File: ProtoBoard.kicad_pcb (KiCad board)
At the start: 4 copper layers, 50 x 35 mm, 52 parts, among them IC1 L9110S, IC2 L9110S, IC3 L9110S, J1 Conn_01x02_Female, J11 Conn_01x10_Female, J2 Conn_01x08_Female, J3 I2C_STANDARDQWIIC, J4 Conn_01x10_Female, J5 Conn_01x05_Female, J6 Conn_01x05_Female, J7 Conn_01x10_Female, J8 Conn_01x05_Female, J9 Conn_01x10_Female, U1 ESP32-WROOM-32D, U10 SY6280AAC, U2 CD74HC4067SM, U3 LM1084-5.0, U4 CD74HC4067SM, U6 LM1084-3.3, U7 SY6280AAC, U8 SY6280AAC, U9 SY6280AAC

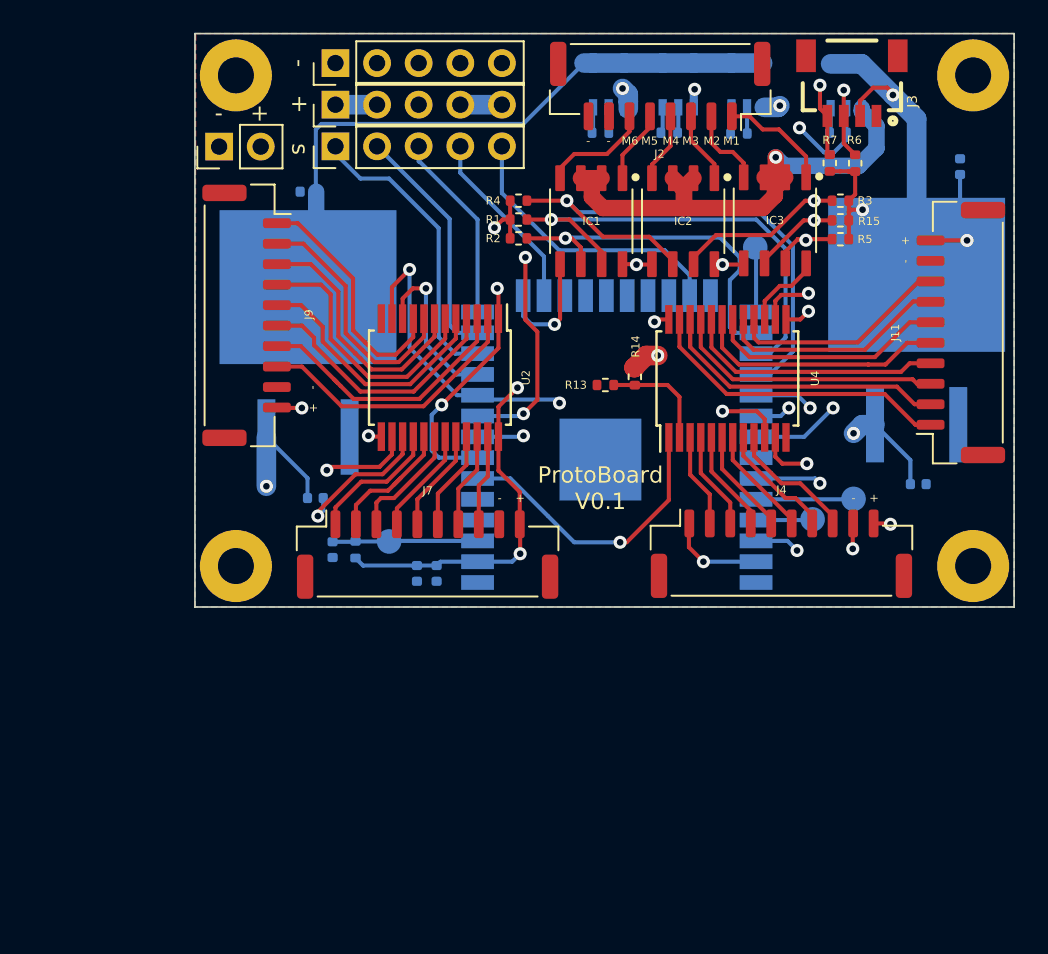
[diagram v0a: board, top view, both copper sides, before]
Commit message: Add bms + switch to esp32s3 + USB C + 8 LRA driver
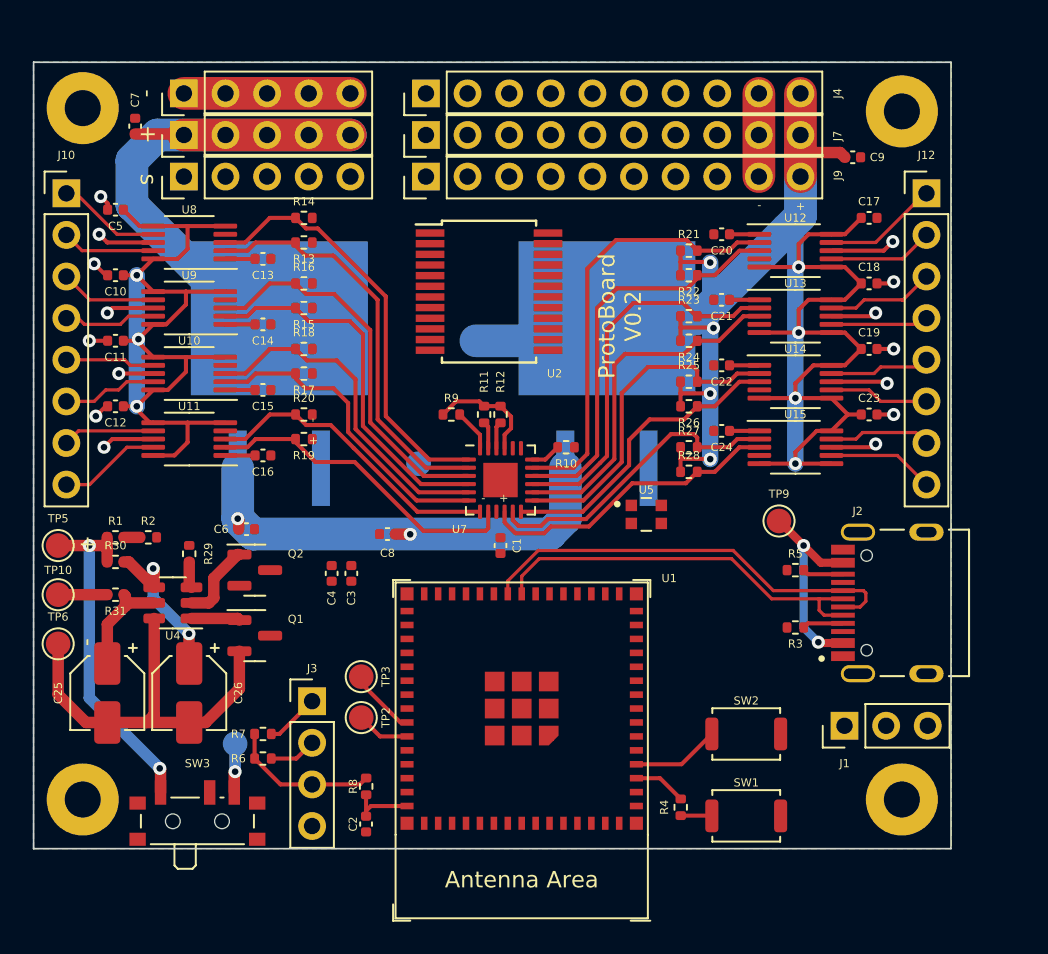
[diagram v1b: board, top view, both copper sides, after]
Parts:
- removed IC1, IC2, IC3: L9110S, footprints:SOIC127P600X150-8
- removed J11: Conn_01x10_Female, Connector_JST:JST_GH_SM10B-GHS-TB_1x10-1MP_P1.25mm_Horizontal
- removed TP1: TestPoint, TestPoint:TestPoint_Pad_D1.5mm
- added C1: 10uF, Capacitor_SMD:C_0402_1005Metric, F.Cu at (76.2, 91.2)
- added C10: 10uF, Capacitor_SMD:C_0402_1005Metric, F.Cu at (52.6, 74.8)
- added C11: 10uF, Capacitor_SMD:C_0402_1005Metric, F.Cu at (52.6, 78.8)
- added C12: 10uF, Capacitor_SMD:C_0402_1005Metric, F.Cu at (52.6, 82.8)
- added C13: 1uF, Capacitor_SMD:C_0402_1005Metric, F.Cu at (61.6, 73.8)
- added C14: 1uF, Capacitor_SMD:C_0402_1005Metric, F.Cu at (61.6, 77.8)
- added C15: 1uF, Capacitor_SMD:C_0402_1005Metric, F.Cu at (61.6, 81.8)
- added C16: 1uF, Capacitor_SMD:C_0402_1005Metric, F.Cu at (61.6, 85.8)
- added C17: 10uF, Capacitor_SMD:C_0402_1005Metric, F.Cu at (98.7, 71.2)
- added C18: 10uF, Capacitor_SMD:C_0402_1005Metric, F.Cu at (98.7, 75.2)
- added C19: 10uF, Capacitor_SMD:C_0402_1005Metric, F.Cu at (98.7, 79.2)
- added C20: 1uF, Capacitor_SMD:C_0402_1005Metric, F.Cu at (89.7, 72.2)
- added C21: 1uF, Capacitor_SMD:C_0402_1005Metric, F.Cu at (89.7, 76.2)
- added C22: 1uF, Capacitor_SMD:C_0402_1005Metric, F.Cu at (89.7, 80.2)
- added C23: 10uF, Capacitor_SMD:C_0402_1005Metric, F.Cu at (98.7, 83.2)
- added C24: 1uF, Capacitor_SMD:C_0402_1005Metric, F.Cu at (89.7, 84.2)
- added C25: 0.1uF, Capacitor_SMD:CP_Elec_4x5.4, F.Cu at (52.1, 100.2)
- added C26: 0.1uF, Capacitor_SMD:CP_Elec_4x5.4, F.Cu at (57.1, 100.2)
- added C5: 10uF, Capacitor_SMD:C_0402_1005Metric, F.Cu at (52.6, 70.8)
- added J10: Conn_01x08_Female, Connector_PinHeader_2.54mm:PinHeader_1x08_P2.54mm_Vertical, F.Cu at (49.6, 69.8)
- added J12: Conn_01x08_Female, Connector_PinHeader_2.54mm:PinHeader_1x08_P2.54mm_Vertical, F.Cu at (102.2, 69.8)
- added Q1: HX2300A, Package_TO_SOT_SMD:SOT-23, F.Cu at (61.1, 96.8)
- added Q2: HX2300A, Package_TO_SOT_SMD:SOT-23, F.Cu at (61.1, 92.8)
- added R16: 4.7K, Resistor_SMD:R_0402_1005Metric, F.Cu at (64.2, 75.2)
- added R17: 4.7K, Resistor_SMD:R_0402_1005Metric, F.Cu at (64.2, 80.8)
- added R18: 4.7K, Resistor_SMD:R_0402_1005Metric, F.Cu at (64.2, 79.2)
- added R19: 4.7K, Resistor_SMD:R_0402_1005Metric, F.Cu at (64.2, 84.8)
- added R20: 4.7K, Resistor_SMD:R_0402_1005Metric, F.Cu at (64.2, 83.2)
- added R21: 4.7K, Resistor_SMD:R_0402_1005Metric, F.Cu at (87.7, 73.2)
- added R22: 4.7K, Resistor_SMD:R_0402_1005Metric, F.Cu at (87.7, 74.8)
- added R23: 4.7K, Resistor_SMD:R_0402_1005Metric, F.Cu at (87.7, 77.2)
- added R24: 4.7K, Resistor_SMD:R_0402_1005Metric, F.Cu at (87.7, 78.8)
- added R25: 4.7K, Resistor_SMD:R_0402_1005Metric, F.Cu at (87.7, 81.2)
- added R26: 4.7K, Resistor_SMD:R_0402_1005Metric, F.Cu at (87.7, 82.8)
- added R27: 4.7K, Resistor_SMD:R_0402_1005Metric, F.Cu at (87.7, 85.2)
- added R28: 4.7K, Resistor_SMD:R_0402_1005Metric, F.Cu at (87.7, 86.8)
- added R29: 2K, Resistor_SMD:R_0402_1005Metric, F.Cu at (57.1, 91.8)
- added R30: 330R, Resistor_SMD:R_0402_1005Metric, F.Cu at (52.6, 92.2)
- added R31: 330R, Resistor_SMD:R_0402_1005Metric, F.Cu at (52.6, 94.2)
- added SW1: SW_Push, Button_Switch_SMD:SW_Push_SPST_NO_Alps_SKRK, F.Cu at (91.2, 107.8)
- added SW2: SW_Push, Button_Switch_SMD:SW_Push_SPST_NO_Alps_SKRK, F.Cu at (91.2, 102.8)
- added SW3: SW_SPDT, Button_Switch_SMD:SW_SPDT_PCM12, F.Cu at (57.6, 107.8)
- added TP10: TestPoint, TestPoint:TestPoint_Pad_D1.5mm, F.Cu at (49.1, 94.2)
- added TP5: TestPoint, TestPoint:TestPoint_Pad_D1.5mm, F.Cu at (49.1, 91.2)
- added TP6: TestPoint, TestPoint:TestPoint_Pad_D1.5mm, F.Cu at (49.1, 97.2)
- added TP7: TestPoint, TestPoint:TestPoint_Pad_D1.5mm, B.Cu at (74.7, 78.8)
- added TP8: TestPoint, TestPoint:TestPoint_Pad_D1.5mm, B.Cu at (71.2, 86.2)
- added TP9: TestPoint, TestPoint:TestPoint_Pad_D1.5mm, F.Cu at (93.2, 89.8)
- added U11: DRV2605LDGS, Package_SO:VSSOP-10_3x3mm_P0.5mm, F.Cu at (57.1, 84.8)
- added U12: DRV2605LDGS, Package_SO:VSSOP-10_3x3mm_P0.5mm, F.Cu at (94.2, 73.2)
- added U13: DRV2605LDGS, Package_SO:VSSOP-10_3x3mm_P0.5mm, F.Cu at (94.2, 77.2)
- added U14: DRV2605LDGS, Package_SO:VSSOP-10_3x3mm_P0.5mm, F.Cu at (94.2, 81.2)
- added U15: DRV2605LDGS, Package_SO:VSSOP-10_3x3mm_P0.5mm, F.Cu at (94.2, 85.2)
- added U5: WS2812-2020, WS2812-2020:LED_WS2812-2020, F.Cu at (85.0, 89.3)
- C2, C3, C4, C6, C7, C8, C9, R8, TP2, TP3: moved to F.Cu
- J1: value Conn_01x02_Female -> Conn_01x03_Female; footprint Connector_PinHeader_2.54mm:PinHeader_1x02_P2.54mm_Vertical -> Connector_PinHeader_2.54mm:PinHeader_1x03_P2.54mm_Vertical
- J2: value Conn_01x08_Female -> TYPE-C-31-M-12; footprint Connector_JST:JST_GH_SM08B-GHS-TB_1x08-1MP_P1.25mm_Horizontal -> TYPE-C-31-M-12:HRO_TYPE-C-31-M-12
- J3: value I2C_STANDARDQWIIC -> Conn_01x04_Female; footprint Connectors:1X04_1MM_RA -> Connector_PinHeader_2.54mm:PinHeader_1x04_P2.54mm_Vertical
- J4, J7, J9: footprint Connector_JST:JST_GH_SM10B-GHS-TB_1x10-1MP_P1.25mm_Horizontal -> Connector_PinHeader_2.54mm:PinHeader_1x10_P2.54mm_Vertical
- R1: value 10K -> 5M
- R10: value 3.4K -> 10K; moved to F.Cu
- R11, R12: value 6.8K -> 10K; moved to F.Cu
- R13: value 1M -> 4.7K
- R14: value 5M -> 4.7K
- R15: value 10K -> 4.7K
- R2: value 10K -> 1M
- R3, R5: value 10K -> 5K1
- R9: value 1.7K -> 10K; moved to F.Cu
- TP4: value TestPoint -> TP
- U1: value ESP32-WROOM-32D -> ESP32-S3-MINI-1; footprint RF_Module:ESP32-WROOM-32 -> Espressif:ESP32-S3-MINI-1; moved to F.Cu
- U10, U8, U9: value SY6280AAC -> DRV2605LDGS; footprint footprints:SY6280AAC -> Package_SO:VSSOP-10_3x3mm_P0.5mm; moved to F.Cu
- U4: value CD74HC4067SM -> HY2120; footprint Package_SO:SSOP-24_5.3x8.2mm_P0.65mm -> Package_TO_SOT_SMD:SOT-23-6
- U7: value SY6280AAC -> TCA9548ARGER; footprint footprints:SY6280AAC -> Package_DFN_QFN:Texas_RGE0024C_EP2.1x2.1mm; moved to F.Cu
- moved J1 52.0 mm to (97.2, 102.2)
- moved R6 51.3 mm to (61.6, 104.2), turned to 180 degrees
- moved R7 49.1 mm to (61.6, 102.8), turned to 180 degrees
- moved J3 48.6 mm to (64.7, 100.8), turned to 0 degrees
- moved TP4 43.9 mm to (60.0, 103.3)
- moved U10 38.3 mm to (57.1, 80.8), turned to 180 degrees
- moved R4 38.3 mm to (87.2, 107.2), turned to -90 degrees
- moved U4 36.5 mm to (56.1, 94.8), turned to 180 degrees
- moved J4 35.5 mm to (71.6, 63.6), turned to 90 degrees
- moved J2 35.5 mm to (102.2, 94.8), turned to 90 degrees
- moved R15 33.2 mm to (64.2, 76.8), turned to 180 degrees
- moved TP2 32.9 mm to (67.7, 101.8), turned to 0 degrees
- moved C8 32.5 mm to (69.2, 90.5), turned to 180 degrees
- moved U7 32.0 mm to (76.2, 87.2), turned to 0 degrees
- moved U8 31.4 mm to (57.1, 72.8), turned to 180 degrees
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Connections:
- C6 pad 1: +BATT -> /VIN
- C8 pad 1: +BATT -> /VIN
- J1 pad 2: +BATT -> /RGB_EXT
- J3 pad 1: GND -> /I2C_SCL
- J3 pad 2: +3V3 -> /I2C_SDA
- J3 pad 3: /I2C_SDA -> +3V3
- J3 pad 4: /I2C_SCL -> GND
- J4 pad 1: /RGB -> /CH16
- J6 pad 1: /POWER2 -> +5V
- J6 pad 2: /POWER2 -> +5V
- J6 pad 3: /POWER3 -> +5V
- J6 pad 4: /POWER1 -> +5V
- J6 pad 5: /POWER1 -> +5V
- R1 pad 1: /LRA5 -> +BATT
- R1 pad 2: +3V3 -> /BAT_SENSE
- R10 pad 1: GND -> +3V3
- R11 pad 1: GND -> +3V3
- R12 pad 1: GND -> +3V3
- R13 pad 1: Net-(R13-Pad1) -> +3V3
- R13 pad 2: GND -> /LRA/SC0
- R14 pad 1: Net-(R13-Pad1) -> +3V3
- R14 pad 2: +BATT -> /LRA/SD0
- R15 pad 1: /LRA2 -> +3V3
- R15 pad 2: +3V3 -> /LRA/SC1
- R2 pad 1: /LRA6 -> /BAT_SENSE
- R2 pad 2: +3V3 -> GND
- R3 pad 1: /LRA3 -> GND
- R3 pad 2: +3V3 -> Net-(J2-PadA5)
- R4 pad 1: /LRA4 -> +3V3
- R4 pad 2: +3V3 -> /EN
- R5 pad 1: /LRA1 -> Net-(J2-PadB5)
- R5 pad 2: +3V3 -> GND
- R9 pad 1: GND -> +3V3
- TP4 pad 1: /BOOT0 -> Net-(SW3-Pad3)
- U1 pad 10: /SEL2 -> /ButJ
- U1 pad 11: /SEL1 -> /ButC
- U1 pad 15: GND -> /Servo4
- U1 pad 16: /Servo4 -> /Servo5
- U1 pad 17: unconnected-(U1-Pad17) -> /I2C_SDA
- U1 pad 18: unconnected-(U1-Pad18) -> /I2C_SCL
- U1 pad 19: unconnected-(U1-Pad19) -> /RGB
- U1 pad 2: +3V3 -> GND
- U1 pad 20: unconnected-(U1-Pad20) -> /ButB
- U1 pad 21: unconnected-(U1-Pad21) -> /Menu
- U1 pad 22: unconnected-(U1-Pad22) -> /ButA
- U1 pad 23: /Servo5 -> /USB_DN
- U1 pad 24: unconnected-(U1-Pad24) -> /USB_DP
- U1 pad 25: /BOOT0 -> /SEL1
- U1 pad 26: /LRA6 -> /SEL2
- U1 pad 27: /LRA5 -> unconnected-(U1-Pad27)
- U1 pad 28: /LRA4 -> unconnected-(U1-Pad28)
- U1 pad 29: /LRA2 -> unconnected-(U1-Pad29)
- U1 pad 3: /EN -> +3V3
- U1 pad 30: /LRA1 -> unconnected-(U1-Pad30)
- U1 pad 31: /LRA3 -> /IN_TRIG0
- U1 pad 32: unconnected-(U1-Pad32) -> /IN_TRIG1
- U1 pad 33: /I2C_SDA -> /IN_TRIG2
- U1 pad 34: /RXD0 -> /IN_TRIG3
- U1 pad 35: /TXD0 -> /IN_TRIG4
- U1 pad 36: /I2C_SCL -> /IN_TRIG5
- U1 pad 37: /RGB -> /IN_TRIG6
- U1 pad 38: GND -> /IN_TRIG7
- U1 pad 39: GND -> /TXD0
- U1 pad 4: unconnected-(U1-Pad4) -> /BOOT
- U1 pad 5: unconnected-(U1-Pad5) -> /BAT_SENSE
- U1 pad 6: /COM2 -> /COM1
- U1 pad 7: /COM1 -> /CH16
- U1 pad 8: /SEL3 -> /JoyX
- U1 pad 9: /SEL4 -> /JoyY
- U10 pad 1: /POWER1 -> Net-(C15-Pad1)
- U10 pad 2: GND -> /LRA/SC2
- U10 pad 3: Net-(R12-Pad2) -> /LRA/SD2
- U10 pad 4: +5V -> /IN_TRIG2
- U10 pad 5: +5V -> +3V3
- U3 pad 3: +BATT -> /VIN
- U4 pad 1: /COM2 -> /OD
- U4 pad 2: Net-(R13-Pad1) -> /OC
- U4 pad 3: /ButA -> Net-(R29-Pad2)
- U4 pad 4: /Menu -> Net-(C26-Pad1)
- U4 pad 5: /ButB -> /HY_VDD
- U4 pad 6: /ButC -> -BATT
- U6 pad 3: +BATT -> /VIN
- U7 pad 1: /POWER4 -> /LRA/SD0
- U7 pad 2: GND -> /LRA/SC0
- U7 pad 3: Net-(R9-Pad2) -> /LRA/SD1
- U7 pad 4: +3V3 -> /LRA/SC1
- U7 pad 5: +3V3 -> /LRA/SD2
- U8 pad 1: /POWER3 -> Net-(C13-Pad1)
- U8 pad 2: GND -> /LRA/SC0
- U8 pad 3: Net-(R10-Pad2) -> /LRA/SD0
- U8 pad 4: +5V -> /IN_TRIG0
- U8 pad 5: +5V -> +3V3
- U9 pad 1: /POWER2 -> Net-(C14-Pad1)
- U9 pad 2: GND -> /LRA/SC1
- U9 pad 3: Net-(R11-Pad2) -> /LRA/SD1
- U9 pad 4: +5V -> /IN_TRIG1
- U9 pad 5: +5V -> +3V3
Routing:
- net /SEL3: track 69.0 -> 0.00 mm, vias 3 -> 0
- net +BATT: track 86.5 -> 21.4 mm, vias 3 -> 2
- net +3V3: track 141.5 -> 192.3 mm, vias 9 -> 11
- net /SEL4: track 44.1 -> 0.00 mm, vias 4 -> 0
- net /SEL2: track 38.7 -> 0.00 mm, vias 3 -> 0
- net /I2C_SDA: track 40.9 -> 2.89 mm, vias 2 -> 0
- net /I2C_SCL: track 39.7 -> 3.32 mm, vias 2 -> 0
- net /SEL1: track 35.3 -> 0.00 mm, vias 2 -> 0
- net /LRA4: track 34.9 -> 0.00 mm, vias 1 -> 0
- net /POWER4: track 32.6 -> 0.00 mm, vias 1 -> 0
- net /POWER2: track 32.0 -> 0.00 mm, vias 1 -> 0
- net /LRA3: track 30.2 -> 0.00 mm, vias 2 -> 0
- net /LRA5: track 28.8 -> 0.00 mm, vias 1 -> 0
- net /VIN: track 0.00 -> 28.5 mm, vias 0 -> 2
- net /LRA/SC4: track 0.00 -> 26.7 mm
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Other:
- board size 50 x 35 mm -> 56 x 48 mm
- board text added: "ProtoBoard V0.2"
- board text removed: "M1"
- board text removed: "M2"
- board text removed: "M3"
- board text removed: "M4"
- board text removed: "M5"
- board text removed: "M6"
- board text removed: "ProtoBoard V0.1"

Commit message: Routing WIP
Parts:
- moved C4 24.8 mm to (87.5, 104.8), turned to 0 degrees
- moved C3 23.1 mm to (87.5, 103.7), turned to 0 degrees
- moved C1 9.81 mm to (71.2, 82.8), turned to 90 degrees
- moved U5 9.37 mm to (91.0, 96.5), turned to 180 degrees
- moved C6 6.41 mm to (67.0, 90.5)
- moved SW2 1.90 mm to (91.2, 100.8)
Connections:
- J4 pad 1: /CH16 -> /GPIO
- J7 pad 1: /CH16 -> /CH7
- J7 pad 2: /CH15 -> /CH6
- J7 pad 3: /CH14 -> /CH4
- J7 pad 4: /CH13 -> /CH2
- J7 pad 5: /CH12 -> /CH9
- J7 pad 7: /CH10 -> /CH13
- J7 pad 8: /CH9 -> /CH15
- J9 pad 1: /CH1 -> /CH8
- J9 pad 2: /CH2 -> /CH5
- J9 pad 4: /CH4 -> /CH1
- J9 pad 5: /CH5 -> /CH10
- J9 pad 6: /CH6 -> /CH12
- J9 pad 7: /CH7 -> /CH14
- J9 pad 8: /CH8 -> /CH16
- U1 pad 10: /ButJ -> /IN_TRIG5
- U1 pad 11: /ButC -> /IN_TRIG4
- U1 pad 12: /Servo1 -> /JoyX
- U1 pad 13: /Servo2 -> /JoyY
- U1 pad 14: /Servo3 -> /ButJ
- U1 pad 15: /Servo4 -> /ButC
- U1 pad 16: /Servo5 -> unconnected-(U1-Pad16)
- U1 pad 17: /I2C_SDA -> /ButB
- U1 pad 18: /I2C_SCL -> /Menu
- U1 pad 19: /RGB -> /ButA
- U1 pad 20: /ButB -> /GPIO
- U1 pad 21: /Menu -> /I2C_SCL
- U1 pad 22: /ButA -> /I2C_SDA
- U1 pad 25: /SEL1 -> /SEL3
- U1 pad 26: /SEL2 -> /SEL4
- U1 pad 27: unconnected-(U1-Pad27) -> /SEL2
- U1 pad 28: unconnected-(U1-Pad28) -> /SEL1
- U1 pad 30: unconnected-(U1-Pad30) -> /Servo5
- U1 pad 31: /IN_TRIG0 -> /Servo4
- U1 pad 32: /IN_TRIG1 -> /Servo3
- U1 pad 33: /IN_TRIG2 -> /Servo2
- U1 pad 34: /IN_TRIG3 -> /Servo1
- U1 pad 35: /IN_TRIG4 -> /IN_TRIG0
- U1 pad 36: /IN_TRIG5 -> /IN_TRIG1
- U1 pad 37: /IN_TRIG6 -> /IN_TRIG2
- U1 pad 38: /IN_TRIG7 -> /IN_TRIG3
- U1 pad 41: /SEL3 -> unconnected-(U1-Pad41)
- U1 pad 44: /SEL4 -> unconnected-(U1-Pad44)
- U1 pad 7: /CH16 -> /RGB
- U1 pad 8: /JoyX -> /IN_TRIG7
- U1 pad 9: /JoyY -> /IN_TRIG6
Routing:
- net +3V3: track 192.3 -> 353.6 mm, vias 11 -> 21
- net /COM1: track 0.00 -> 44.5 mm, vias 0 -> 3
- net /JoyX: track 0.00 -> 42.3 mm, vias 0 -> 1
- net /JoyY: track 0.00 -> 41.3 mm, vias 0 -> 1
- net /ButJ: track 0.00 -> 40.7 mm, vias 0 -> 1
- net /IN_TRIG0: track 0.00 -> 39.9 mm, vias 0 -> 2
- net /IN_TRIG1: track 0.00 -> 38.4 mm, vias 0 -> 2
- net /ButC: track 0.00 -> 38.0 mm, vias 0 -> 1
- net /BAT_SENSE: track 0.98 -> 38.5 mm, vias 0 -> 2
- net /GPIO: track 0.00 -> 37.3 mm, vias 0 -> 1
- net /ButA: track 0.00 -> 37.2 mm, vias 0 -> 1
- net /Servo1: track 0.00 -> 35.7 mm, vias 0 -> 1
- net /ButB: track 0.00 -> 35.6 mm, vias 0 -> 1
- net /I2C_SCL: track 3.32 -> 38.8 mm, vias 0 -> 3
- net /I2C_SDA: track 2.89 -> 38.1 mm, vias 0 -> 2
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
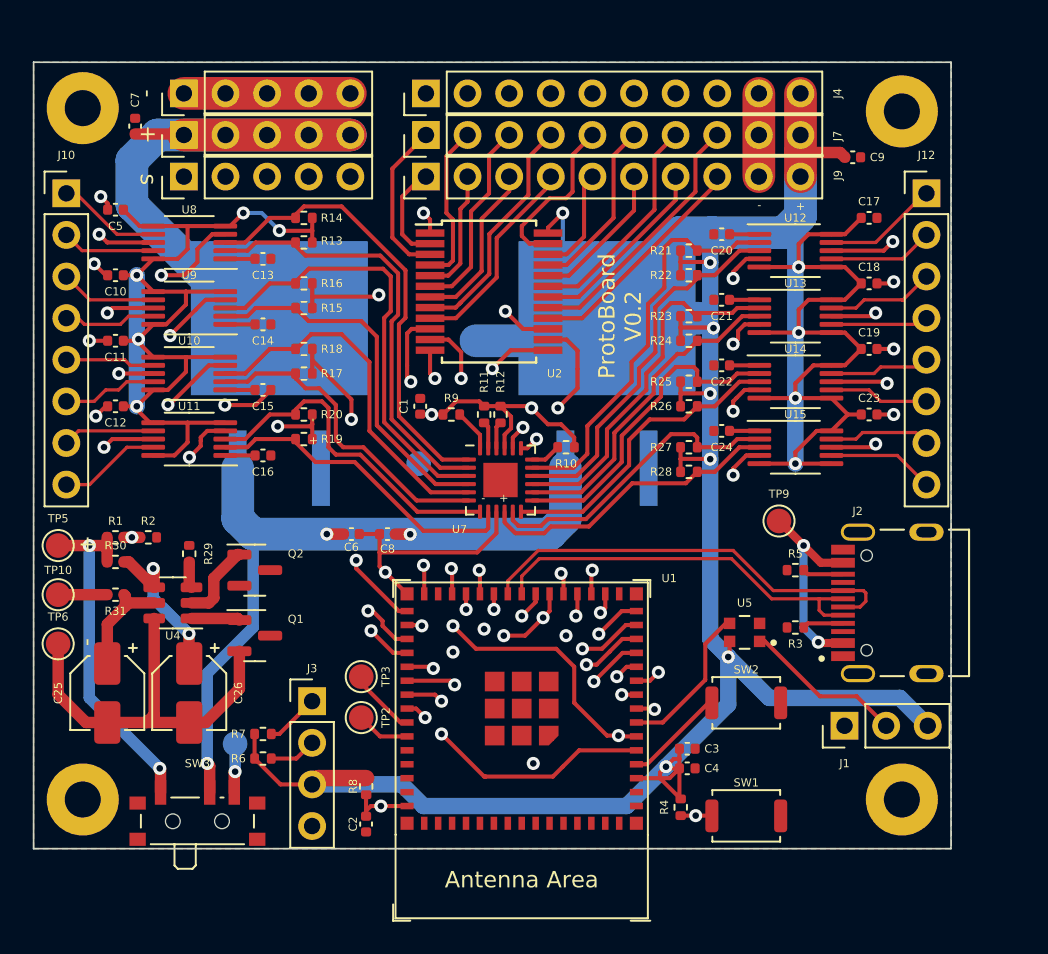
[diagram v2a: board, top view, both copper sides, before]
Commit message: Routing done, silkscreen cleaning, update README, remove old files
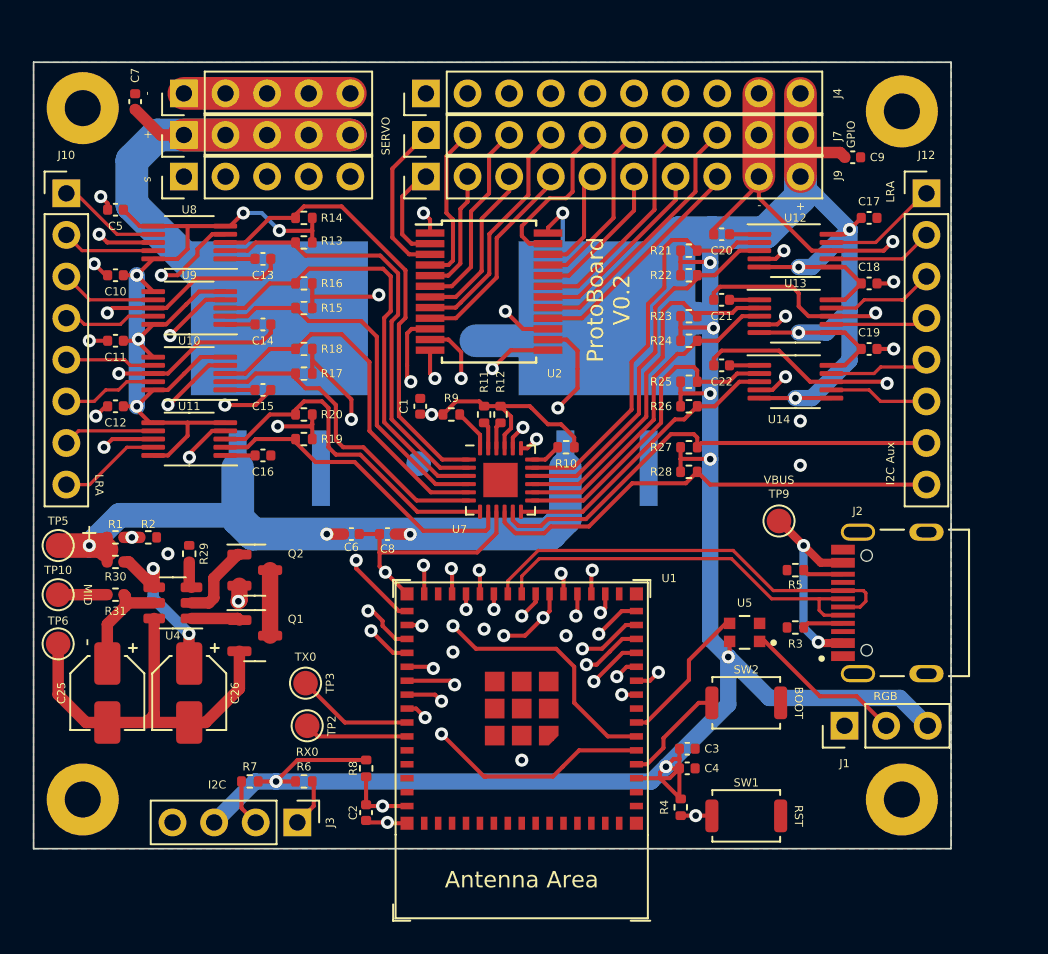
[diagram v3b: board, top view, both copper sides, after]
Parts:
- removed C23: 10uF, Capacitor_SMD:C_0402_1005Metric
- removed C24: 1uF, Capacitor_SMD:C_0402_1005Metric
- removed SW3: SW_SPDT, Button_Switch_SMD:SW_SPDT_PCM12
- removed TP4: TP, TestPoint:TestPoint_Pad_D1.5mm
- removed U15: DRV2605LDGS, Package_SO:VSSOP-10_3x3mm_P0.5mm
- moved J3 7.45 mm to (63.8, 108.2), turned to -90 degrees
- moved TP3 3.42 mm to (64.2, 99.7)
- moved TP2 3.34 mm to (64.3, 102.2)
- moved R7 3.01 mm to (60.9, 105.7), turned to 0 degrees
- moved R6 2.87 mm to (64.2, 105.7)
- moved C7 1.50 mm to (53.9, 64.2)
- moved R8 1.10 mm to (68.0, 104.8)
- moved C2 0.70 mm to (67.9, 107.5)
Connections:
- C6 pad 1: /VIN -> +BATT
- C8 pad 1: /VIN -> +BATT
- J12 pad 7: /LRA/OUT7_N -> /LRA/SC7
- J12 pad 8: /LRA/OUT7_P -> /LRA/SD7
- J3 pad 1: /I2C_SCL -> /I2C_SDA
- J3 pad 2: /I2C_SDA -> /I2C_SCL
- U1 pad 8: /IN_TRIG7 -> unconnected-(U1-Pad8)
- U3 pad 3: /VIN -> +BATT
- U6 pad 3: /VIN -> +BATT
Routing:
- net GND: track 69.8 -> 116.4 mm, vias 23 -> 26
- net /VIN: track 45.9 -> 0.00 mm, vias 3 -> 0
- net +BATT: track 21.4 -> 43.3 mm, vias 2 -> 3
- net /IN_TRIG7: track 19.7 -> 0.00 mm, vias 2 -> 0
- net +3V3: track 353.6 -> 339.4 mm
- net /LRA/SC7: track 18.9 -> 29.0 mm
- net /LRA/SD7: track 18.6 -> 28.5 mm
- net /LRA/OUT7_P: track 6.54 -> 0.00 mm
- net /LRA/OUT7_N: track 6.23 -> 0.00 mm
- net Net-(Q1-Pad3): track 0.00 -> 4.00 mm
- net /IN_TRIG6: track 24.7 -> 28.2 mm
- net /IN_TRIG5: track 26.2 -> 29.6 mm
- net /IN_TRIG4: track 31.7 -> 34.9 mm
- net /I2C_SCL: track 38.8 -> 42.0 mm
- net /RXD0: track 3.27 -> 6.36 mm
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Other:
- board text added: "3.3V"
- board text added: "BOOT"
- board text added: "GND"
- board text added: "GPIO"
- board text added: "I2C"
- board text added: "I2C Aux"
- board text added: "LRA"
- board text added: "MID"
- board text added: "RGB"
- board text added: "RST"
- board text added: "RX0"
- board text added: "SERVO"
- board text added: "TX0"
- board text added: "VBUS"
